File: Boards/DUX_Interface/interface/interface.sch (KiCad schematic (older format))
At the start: 20 parts, among them J1 MM_F_VT_20, J2 MM_F_VT_20, J3 MM_F_VT_04, J4 MM_F_VT_10, J5 MM_F_VT_04, J7 Ampseal_35_VT, J8 MicroFit_RA_V_2, U1 Nanofit_12, U2 Nanofit_4, U3 Nanofit_4, U4 Nanofit_10, U5 RJ45_VT, U6 RJ45_VT

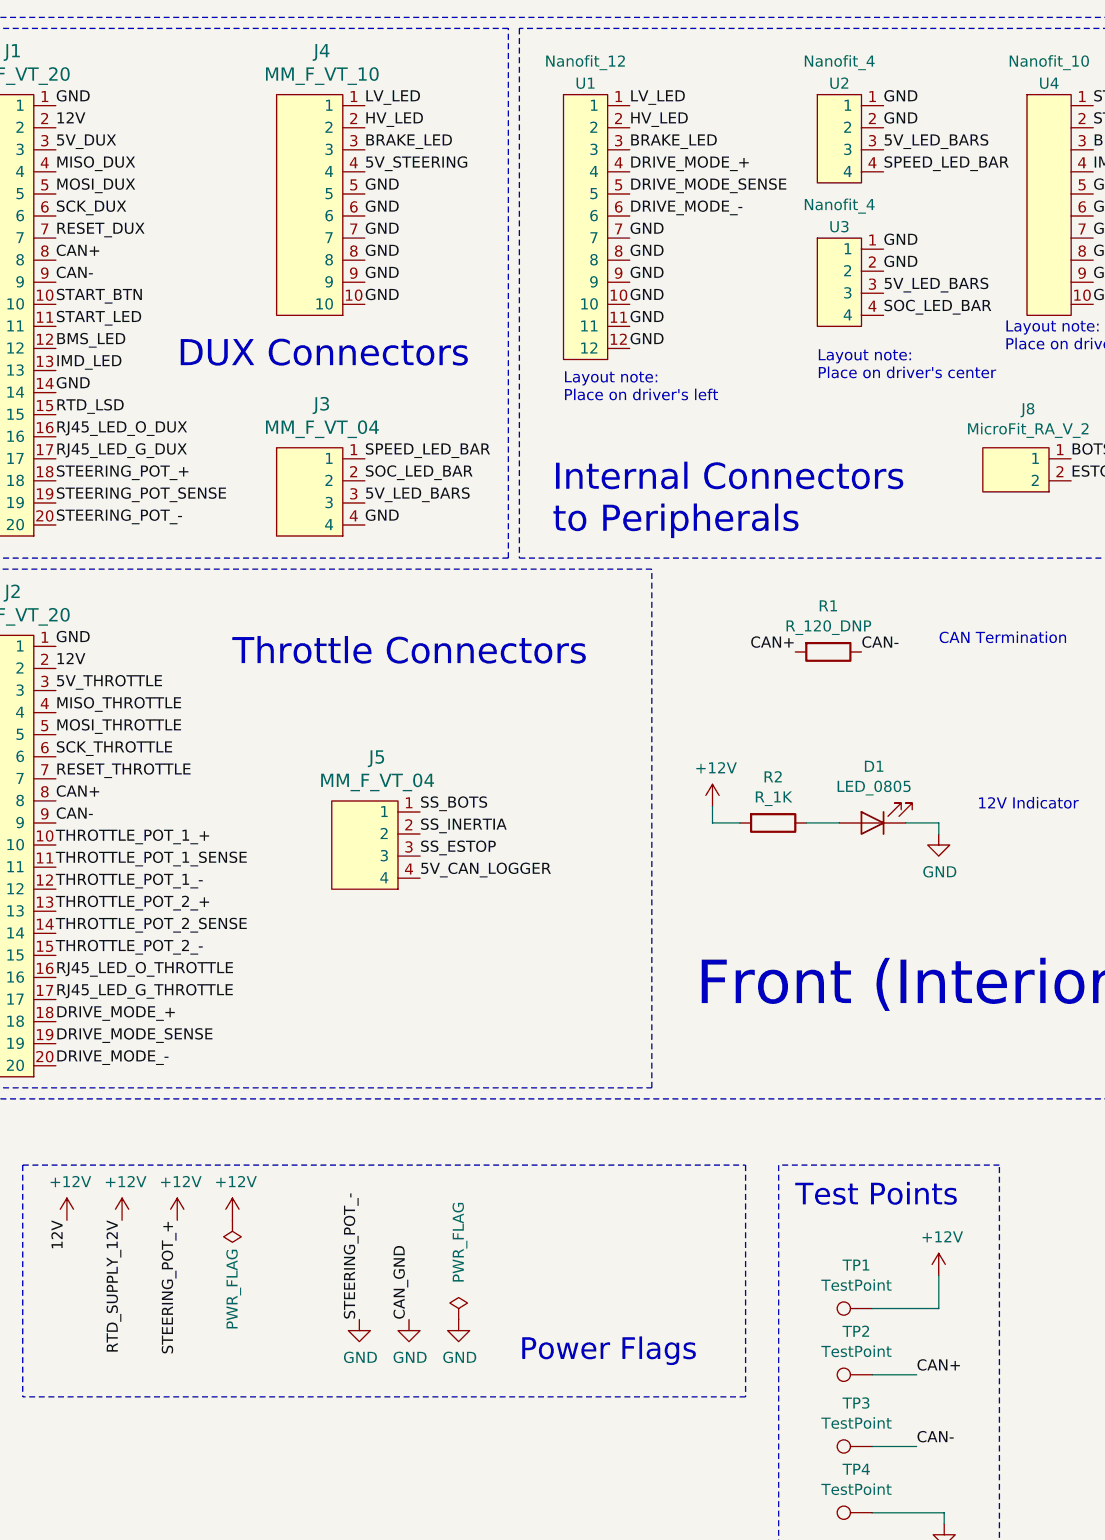
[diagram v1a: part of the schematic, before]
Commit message: schematic and layout fixes
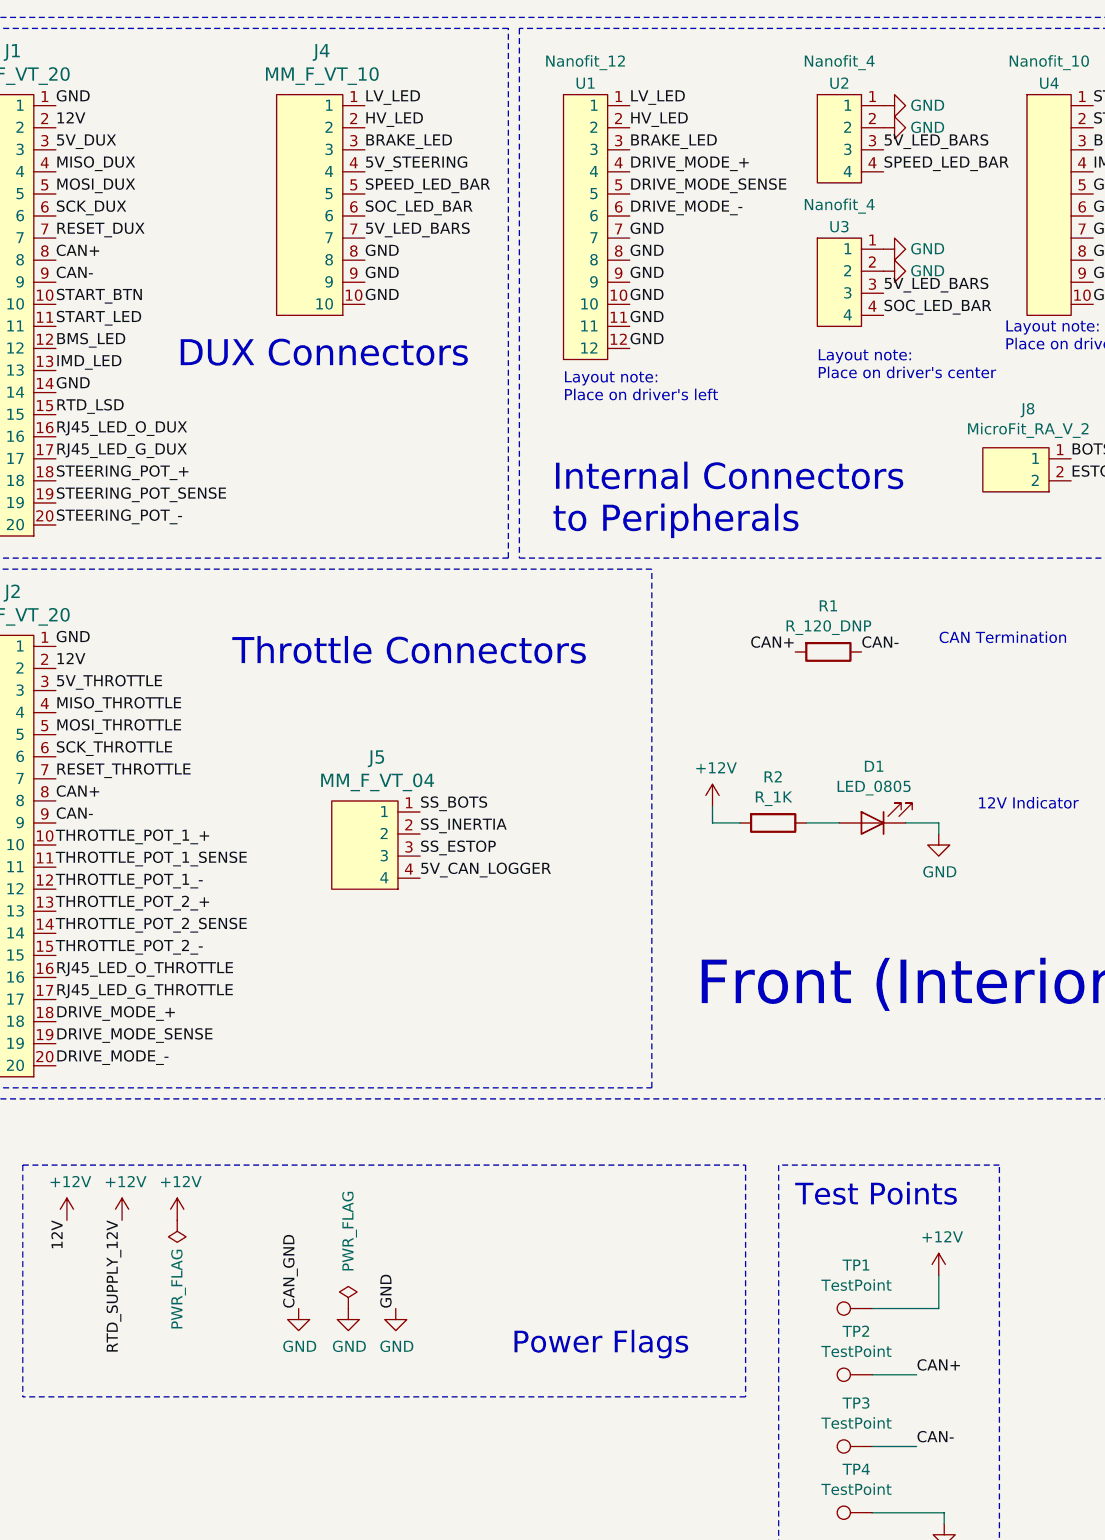
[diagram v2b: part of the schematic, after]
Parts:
- removed J3: MM_F_VT_04, footprints:micromatch_female_vert_4, symbol formula:MM_F_VT_04
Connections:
- net +12V: no longer J1.18, J7.16
- net 5V_LED_BARS: now also J4.7
- net GND: no longer J1.20, J4.5, J4.6, J4.7, J7.18
- net SOC_LED_BAR: now also J4.6
- net SPEED_LED_BAR: now also J4.5
- new net STEERING_POT_+: J1.18, J7.16
- new net STEERING_POT_-: J1.20, J7.18
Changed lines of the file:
@@
-$EndComp
-$Comp
-L formula:MM_F_VT_04 J3
-U 1 1 5DC9CE0A
-P 2200 2700
-F 0 "J3" H 2256 3147 60  0000 C CNN
-F 1 "MM_F_VT_04" H 2256 3041 60  0000 C CNN
-F 2 "footprints:micromatch_female_vert_4" H 2000 3800 60  0001 C CNN
-F 3 "http://www.te.com/commerce/DocumentDelivery/DDEController?Action=showdoc&DocId=Customer+Drawing%7F338068%7FF1%7Fpdf%7FEnglish%7FENG_CD_338068_F1.pdf%7F338068-4" H 2100 3900 60  0001 C CNN
-F 4 "TE" H 2300 4100 60  0001 C CNN "MFN"
-F 5 "338068-4" H 2400 4200 60  0001 C CNN "MPN"
-F 6 "http://www.te.com/global-en/product-338068-4.html" H 2200 4000 60  0001 C CNN "PurchasingLink"
-	1    2200 2700
-	1    0    0    -1
 $EndComp
 $Comp
@@
 Text Label 1050 2800 0    50   ~ 0
 STEERING_POT_-
-Text Label 2450 2500 0    50   ~ 0
-SPEED_LED_BAR
-Text Label 2450 2600 0    50   ~ 0
-SOC_LED_BAR
-Text Label 2450 2700 0    50   ~ 0
-5V_LED_BARS
-Text Label 2450 2800 0    50   ~ 0
-GND
 Text Label 2700 4100 0    50   ~ 0
 SS_BOTS
@@
 Text Label 2450 1200 0    50   ~ 0
 5V_STEERING
-Text Label 2450 1300 0    50   ~ 0
-GND
-Text Label 2450 1400 0    50   ~ 0
-GND
-Text Label 2450 1500 0    50   ~ 0
-GND
 Text Label 2450 1600 0    50   ~ 0
 GND
@@
 GND
 Text Label 2450 1800 0    50   ~ 0
-GND
-Text Label 4800 900  0    50   ~ 0
-GND
-Text Label 4800 1000 0    50   ~ 0
-GND
-Text Label 4800 1550 0    50   ~ 0
-GND
-Text Label 4800 1650 0    50   ~ 0
 GND
 Text Label 4800 1100 0    50   ~ 0
@@
 L power:GND #PWR03
 U 1 1 5DCFDED7
-P 2650 6400
-F 0 "#PWR03" H 2650 6150 50  0001 C CNN
-F 1 "GND" H 2655 6227 50  0000 C CNN
-F 2 "" H 2650 6400 50  0001 C CNN
-F 3 "" H 2650 6400 50  0001 C CNN
-	1    2650 6400
-	1    0    0    -1
-$EndComp
-Text Label 2650 6400 1    50   ~ 0
+P 2150 6350
+F 0 "#PWR03" H 2150 6100 50  0001 C CNN
+F 1 "GND" H 2155 6177 50  0000 C CNN
+F 2 "" H 2150 6350 50  0001 C CNN
+F 3 "" H 2150 6350 50  0001 C CNN
+	1    2150 6350
+	1    0    0    -1
+$EndComp
+Text Label 2150 6350 1    50   ~ 0
 CAN_GND
-Text Notes 3150 6600 0    98   ~ 0
+Text Notes 3115 6570 0    98   ~ 0
 Power Flags\n
 $Comp
 L power:PWR_FLAG #FLG01
 U 1 1 5DCFEE19
-P 1850 5950
-F 0 "#FLG01" H 1850 6025 50  0001 C CNN
-F 1 "PWR_FLAG" V 1850 6078 50  0000 L CNN
-F 2 "" H 1850 5950 50  0001 C CNN
-F 3 "~" H 1850 5950 50  0001 C CNN
-	1    1850 5950
+P 1600 5950
+F 0 "#FLG01" H 1600 6025 50  0001 C CNN
+F 1 "PWR_FLAG" V 1600 6078 50  0000 L CNN
+F 2 "" H 1600 5950 50  0001 C CNN
+F 3 "~" H 1600 5950 50  0001 C CNN
+	1    1600 5950
 	-1   0    0    1
 $EndComp
@@
 L power:+12V #PWR04
 U 1 1 5DCFF24F
-P 1850 5950
-F 0 "#PWR04" H 1850 5800 50  0001 C CNN
-F 1 "+12V" H 1865 6123 50  0000 C CNN
-F 2 "" H 1850 5950 50  0001 C CNN
-F 3 "" H 1850 5950 50  0001 C CNN
-	1    1850 5950
+P 1600 5950
+F 0 "#PWR04" H 1600 5800 50  0001 C CNN
+F 1 "+12V" H 1615 6123 50  0000 C CNN
+F 2 "" H 1600 5950 50  0001 C CNN
+F 3 "" H 1600 5950 50  0001 C CNN
+	1    1600 5950
 	1    0    0    -1
 $EndComp
@@
 L power:PWR_FLAG #FLG02
 U 1 1 5DD01903
-P 2875 6400
-F 0 "#FLG02" H 2875 6475 50  0001 C CNN
-F 1 "PWR_FLAG" V 2875 6750 50  0000 C CNN
-F 2 "" H 2875 6400 50  0001 C CNN
-F 3 "~" H 2875 6400 50  0001 C CNN
-	1    2875 6400
+P 2375 6350
+F 0 "#FLG02" H 2375 6425 50  0001 C CNN
+F 1 "PWR_FLAG" V 2375 6700 50  0000 C CNN
+F 2 "" H 2375 6350 50  0001 C CNN
+F 3 "~" H 2375 6350 50  0001 C CNN
+	1    2375 6350
 	1    0    0    -1
 $EndComp
@@
 L power:GND #PWR05
 U 1 1 5DD0198E
-P 2875 6400
-F 0 "#PWR05" H 2875 6150 50  0001 C CNN
-F 1 "GND" H 2880 6227 50  0000 C CNN
-F 2 "" H 2875 6400 50  0001 C CNN
-F 3 "" H 2875 6400 50  0001 C CNN
-	1    2875 6400
+P 2375 6350
+F 0 "#PWR05" H 2375 6100 50  0001 C CNN
+F 1 "GND" H 2380 6177 50  0000 C CNN
+F 2 "" H 2375 6350 50  0001 C CNN
+F 3 "" H 2375 6350 50  0001 C CNN
+	1    2375 6350
 	1    0    0    -1
 $EndComp
@@
 Text Label 10200 2650 0    50   ~ 0
 5V_STEERING
-Text Label 1600 5950 3    50   ~ 0
-STEERING_POT_+
-Text Label 2425 6400 1    50   ~ 0
-STEERING_POT_-
-$Comp
-L power:+12V #PWR0101
-U 1 1 5E63233C
-P 1600 5950
-F 0 "#PWR0101" H 1600 5800 50  0001 C CNN
-F 1 "+12V" H 1615 6123 50  0000 C CNN
-F 2 "" H 1600 5950 50  0001 C CNN
-F 3 "" H 1600 5950 50  0001 C CNN
-	1    1600 5950
-	1    0    0    -1
-$EndComp
-$Comp
-L power:GND #PWR0102
-U 1 1 5E63537E
-P 2425 6400
-F 0 "#PWR0102" H 2425 6150 50  0001 C CNN
-F 1 "GND" H 2430 6227 50  0000 C CNN
-F 2 "" H 2425 6400 50  0001 C CNN
-F 3 "" H 2425 6400 50  0001 C CNN
-	1    2425 6400
-	1    0    0    -1
-$EndComp
 Wire Notes Line
 	4175 5700 4175 6750
@@
 Text Notes 5225 4100 0    50   ~ 0
 12V Indicator
+Text Label 2590 6350 1    50   ~ 0
+GND
+$Comp
+L power:GND #PWR0103
+U 1 1 5E6AE5CE
+P 2590 6350
+F 0 "#PWR0103" H 2590 6100 50  0001 C CNN
+F 1 "GND" H 2595 6177 50  0000 C CNN
+F 2 "" H 2590 6350 50  0001 C CNN
+F 3 "" H 2590 6350 50  0001 C CNN
+	1    2590 6350
+	1    0    0    -1
+$EndComp
+Text Label 2450 1300 0    50   ~ 0
+SPEED_LED_BAR
+Text Label 2450 1400 0    50   ~ 0
+SOC_LED_BAR
+Text Label 2450 1500 0    50   ~ 0
+5V_LED_BARS
+$Comp
+L power:GND #PWR?
+U 1 1 5E6BE8EA
+P 4800 1550
+F 0 "#PWR?" H 4800 1300 50  0001 C CNN
+F 1 "GND" V 4800 1350 50  0000 C CNN
+F 2 "" H 4800 1550 50  0001 C CNN
+F 3 "" H 4800 1550 50  0001 C CNN
+	1    4800 1550
+	0    -1   -1   0
+$EndComp
+$Comp
+L power:GND #PWR?
+U 1 1 5E6BEDD5
+P 4800 1650
+F 0 "#PWR?" H 4800 1400 50  0001 C CNN
+F 1 "GND" V 4800 1450 50  0000 C CNN
+F 2 "" H 4800 1650 50  0001 C CNN
+F 3 "" H 4800 1650 50  0001 C CNN
+	1    4800 1650
+	0    -1   -1   0
+$EndComp
+$Comp
+L power:GND #PWR?
+U 1 1 5E6BFA26
+P 4800 900
+F 0 "#PWR?" H 4800 650 50  0001 C CNN
+F 1 "GND" V 4800 700 50  0000 C CNN
+F 2 "" H 4800 900 50  0001 C CNN
+F 3 "" H 4800 900 50  0001 C CNN
+	1    4800 900
+	0    -1   -1   0
+$EndComp
+$Comp
+L power:GND #PWR?
+U 1 1 5E6BFA2C
+P 4800 1000
+F 0 "#PWR?" H 4800 750 50  0001 C CNN
+F 1 "GND" V 4800 800 50  0000 C CNN
+F 2 "" H 4800 1000 50  0001 C CNN
+F 3 "" H 4800 1000 50  0001 C CNN
+	1    4800 1000
+	0    -1   -1   0
+$EndComp
 $EndSCHEMATC

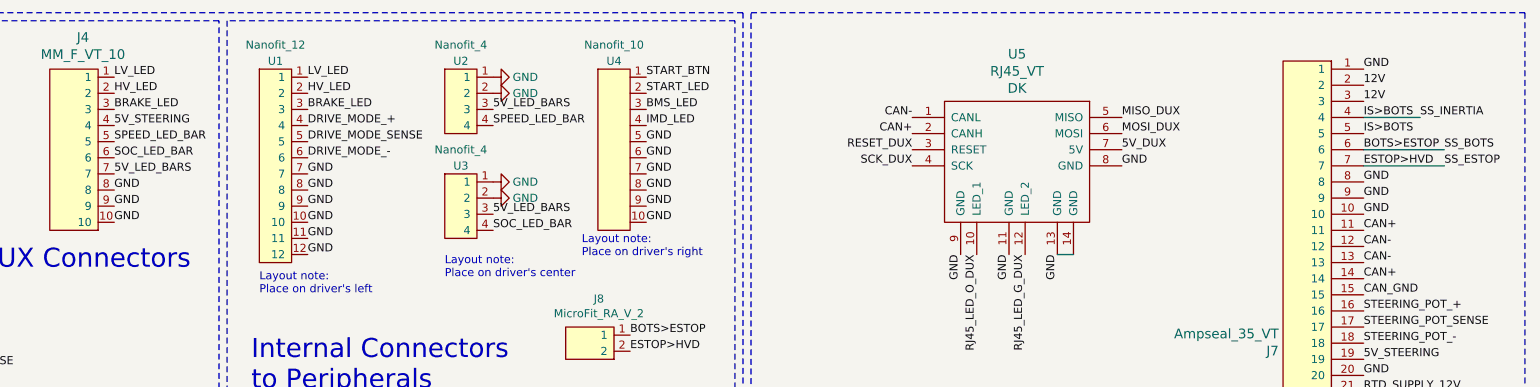
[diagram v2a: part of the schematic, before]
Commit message: fixed connector overlap issues & minor pinout changes
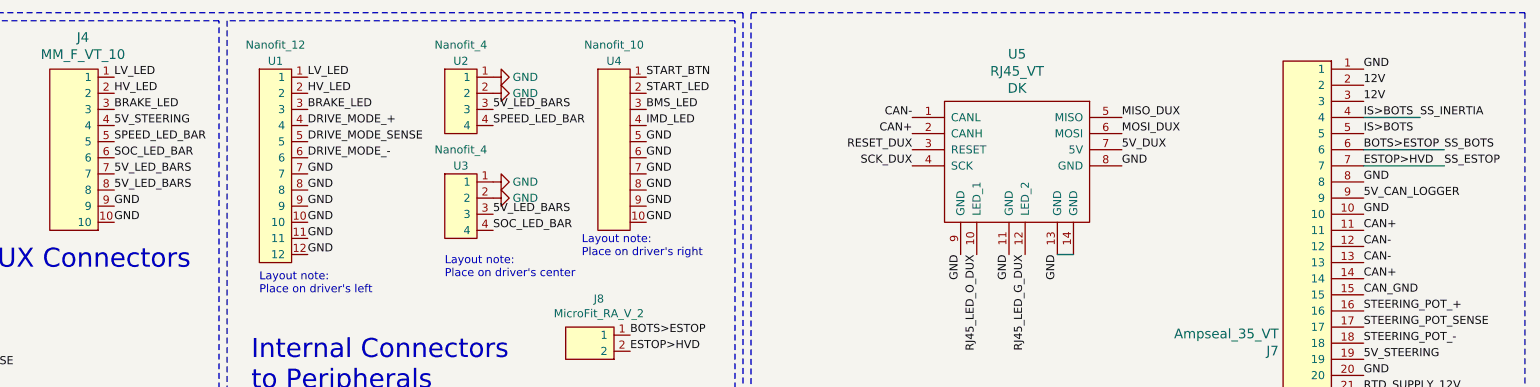
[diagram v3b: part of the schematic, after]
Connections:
- net 5V_CAN_LOGGER: now also J7.9
- net 5V_LED_BARS: now also J4.8
- net GND: no longer J4.8, J7.9
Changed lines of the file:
@@
 Text Label 2450 1200 0    50   ~ 0
 5V_STEERING
-Text Label 2450 1600 0    50   ~ 0
-GND
 Text Label 2450 1700 0    50   ~ 0
 GND
@@
 Text Label 10200 1550 0    50   ~ 0
 GND
-Text Label 10200 1650 0    50   ~ 0
-GND
 Text Label 10200 1750 0    50   ~ 0
 GND
@@
 5V_LED_BARS
 $Comp
-L power:GND #PWR?
+L power:GND #PWR0101
 U 1 1 5E6BE8EA
 P 4800 1550
-F 0 "#PWR?" H 4800 1300 50  0001 C CNN
+F 0 "#PWR0101" H 4800 1300 50  0001 C CNN
 F 1 "GND" V 4800 1350 50  0000 C CNN
 F 2 "" H 4800 1550 50  0001 C CNN
@@
 $EndComp
 $Comp
-L power:GND #PWR?
+L power:GND #PWR0102
 U 1 1 5E6BEDD5
 P 4800 1650
-F 0 "#PWR?" H 4800 1400 50  0001 C CNN
+F 0 "#PWR0102" H 4800 1400 50  0001 C CNN
 F 1 "GND" V 4800 1450 50  0000 C CNN
 F 2 "" H 4800 1650 50  0001 C CNN
@@
 $EndComp
 $Comp
-L power:GND #PWR?
+L power:GND #PWR0104
 U 1 1 5E6BFA26
 P 4800 900
-F 0 "#PWR?" H 4800 650 50  0001 C CNN
+F 0 "#PWR0104" H 4800 650 50  0001 C CNN
 F 1 "GND" V 4800 700 50  0000 C CNN
 F 2 "" H 4800 900 50  0001 C CNN
@@
 $EndComp
 $Comp
-L power:GND #PWR?
+L power:GND #PWR0105
 U 1 1 5E6BFA2C
 P 4800 1000
-F 0 "#PWR?" H 4800 750 50  0001 C CNN
+F 0 "#PWR0105" H 4800 750 50  0001 C CNN
 F 1 "GND" V 4800 800 50  0000 C CNN
 F 2 "" H 4800 1000 50  0001 C CNN
@@
 	0    -1   -1   0
 $EndComp
+Text Label 10200 1650 0    50   ~ 0
+5V_CAN_LOGGER
+Text Label 2450 1600 0    50   ~ 0
+5V_LED_BARS
 $EndSCHEMATC
